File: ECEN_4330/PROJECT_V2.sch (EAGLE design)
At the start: 32 parts

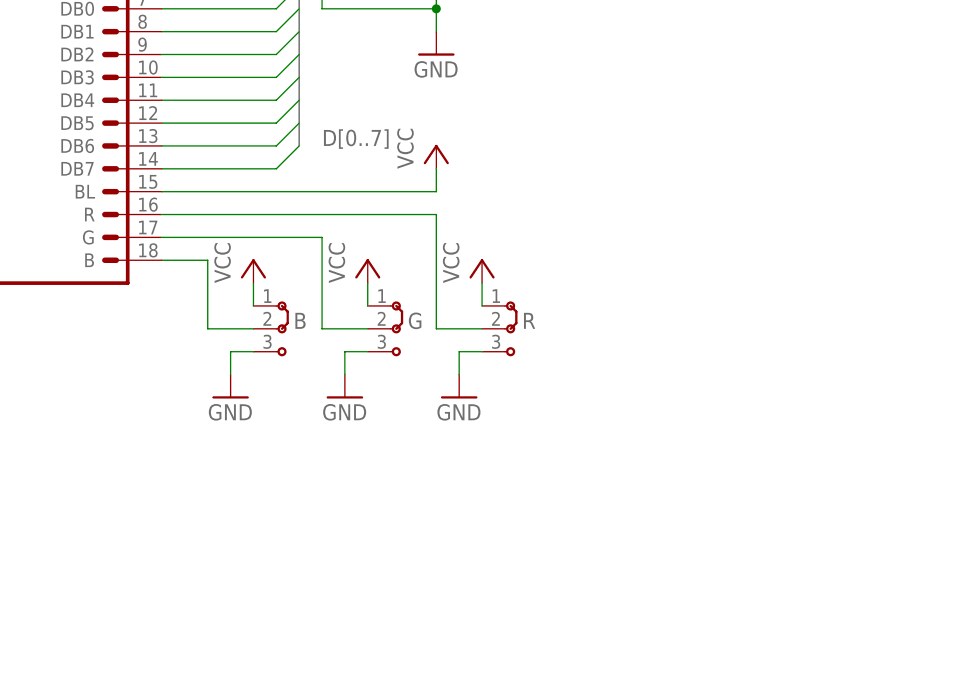
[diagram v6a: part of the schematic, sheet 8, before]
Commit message: Changed lbr to more clearly display specific parts, Added Color select to schematic
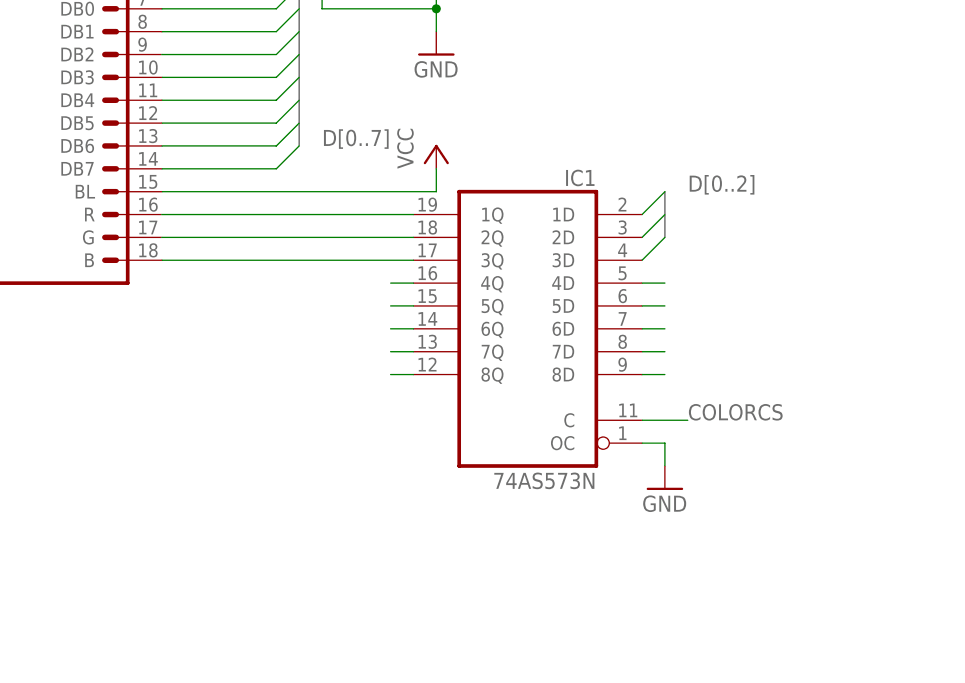
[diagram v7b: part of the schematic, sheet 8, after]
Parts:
- removed B, G, R: (no value), jumper:J2X5MM
- added IC1: 74AS573N, Fuckboiz:74AS573N
- MICROCONTROLLER: device micro-intel:8051P -> Fuckboiz:8051P
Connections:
- removed net R/W: CSLOGICG$1.O6
- new net COLORCS: CSLOGICG$1.O6, IC1A.C
- new net N$2: DEMULTIPLEXERA.C, MICROCONTROLLER.ALE
- new net N$23: IC1A.2Q, LCD.G
- new net N$36: IC1A.6D
- new net N$37: IC1A.7D
- new net N$38: IC1A.8D
- new net N$39: IC1A.4Q
- new net N$40: IC1A.5Q
- new net N$41: IC1A.6Q
- new net N$42: IC1A.7Q
- new net N$46: IC1A.8Q
- net A13: now also CSLOGICG$1.I3
- net ALE: no longer DEMULTIPLEXERA.OC, MICROCONTROLLER.ALE
- net D0: now also IC1A.1D
- net D1: now also IC1A.2D
- net D2: now also IC1A.3D
- net GND: now also DEMULTIPLEXERA.OC, IC1A.OC; no longer B.3, DEMULTIPLEXERA.C, G.3, R.3
- net N$17: now also IC1A.1Q, LCD.R; no longer B.2, LCD.B
- net N$24: now also IC1A.3Q, LCD.B; no longer CSLOGICG$1.O5
- net N$32: now also IC1A.4D; no longer LCD.R, R.2
- net N$34: now also IC1A.5D; no longer G.2, LCD.G
- net P3.5: no longer CSLOGICG$1.I5
- net RD: now also CSLOGICG$1.I5; no longer CSLOGICG$1.I4
- net VCC: no longer B.1, G.1, R.1
- net WR: now also CSLOGICG$1.I4; no longer CSLOGICG$1.I3
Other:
- note added: "= P3.5 & PSEN & A13 & ~A14 & ~A15 & ~WR"
- note added: "= ~P3.5 + ~PSEN + A15 + ~A14 + (WR & RD)"
- note removed: "= TBD"
- note removed: "= ~P3.5 + ~PSEN + A15 + ~A14"
